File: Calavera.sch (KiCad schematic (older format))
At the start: 21 parts, among them Q1 Q_DUAL_NMOS, U1 AT42QT1012, U2 LMV932

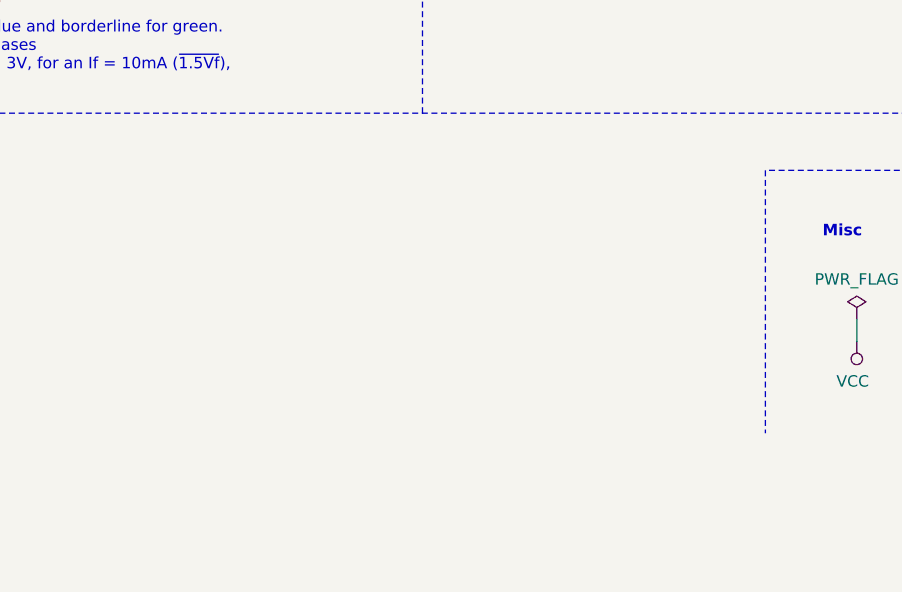
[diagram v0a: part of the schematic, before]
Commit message: Added Silk, Mask and Edge as schematic symbols Updated silk and mask, as they got misaligned Added silk to the nose pad
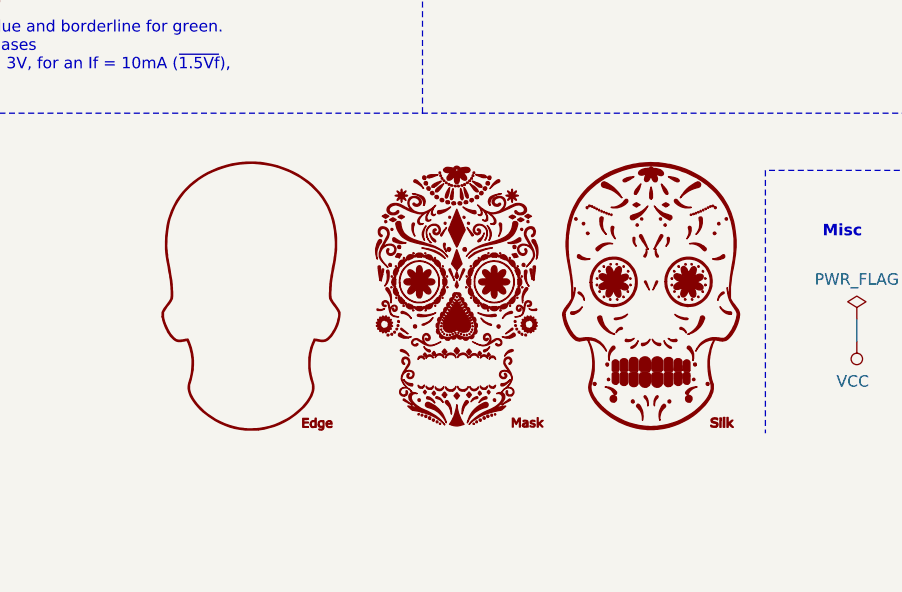
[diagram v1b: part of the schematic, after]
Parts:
- added G2: Edge, Calavera:Calavera_Board_Margins, symbol Calavera:Edge
- added G3: Mask, Calavera:Calavera_SolderMask_1200dpi, symbol Calavera:Mask
- added G4: Silk, Calavera:Calavera_SilkScreen_1200dpi, symbol Calavera:Silk
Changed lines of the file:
@@
 Wire Notes Line
 	500  5100 11200 5100
+$Comp
+L Calavera:Silk G4
+U 1 1 5D5C30EC
+P 9650 5900
+F 0 "G4" H 9650 5339 60  0001 C CNN
+F 1 "Silk" H 9650 6461 60  0001 C CNN
+F 2 "Calavera:Calavera_SilkScreen_1200dpi" H 9650 5900 50  0001 C CNN
+F 3 "" H 9650 5900 50  0001 C CNN
+	1    9650 5900
+	1    0    0    -1
+$EndComp
+$Comp
+L Calavera:Mask G3
+U 1 1 5D5CCE2E
+P 8800 5900
+F 0 "G3" H 9150 5400 60  0001 C CNN
+F 1 "Mask" H 9200 6450 60  0001 C CNN
+F 2 "Calavera:Calavera_SolderMask_1200dpi" H 8800 5900 50  0001 C CNN
+F 3 "" H 8800 5900 50  0001 C CNN
+	1    8800 5900
+	1    0    0    -1
+$EndComp
+$Comp
+L Calavera:Edge G2
+U 1 1 5D5D7396
+P 7900 5900
+F 0 "G2" H 8250 5400 60  0001 C CNN
+F 1 "Edge" H 8300 6450 60  0001 C CNN
+F 2 "Calavera:Calavera_Board_Margins" H 7900 5900 50  0001 C CNN
+F 3 "" H 7900 5900 50  0001 C CNN
+	1    7900 5900
+	1    0    0    -1
+$EndComp
 $EndSCHEMATC

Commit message: v1.0 - Manufactured for the lunch and learn
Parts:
- BT1: MPN (none) -> MP000357; Manufacturer  (none) -> Multicomp
- Q1: MPN (none) -> NX138BKS
- R9: value 2500 -> 2490
- U1: MPN (none) -> AT42QT1012-TSHR
- U2: MPN (none) -> LMV932DR2G
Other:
- note added: "Limiting resistors: voltage is not high enough for Blue and borderline for green.\nI think it's safe to not populate them in these two cases\nTypical red Vf is 1.8V, so in the best case of VDD = 3V, for an If = 10mA (1.5Vf-ish), \nR = 100 to 150Ω"
- note removed: "Limiting resistors: voltage is not high enough for Blue and borderline for green.\nI think it's safe to not populate them in these two cases\nTypical red Vf is 1.8V, so in the best case of VDD = 3V, for an If = 10mA (~1.5Vf), \nR = 150Ω"
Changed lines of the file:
@@
 F 2 "Calavera:CR2032_Multicomp_MP000357_Alternative" V 9450 3960 50  0001 C CNN
 F 3 "~" V 9450 3960 50  0001 C CNN
+F 4 "MP000357" H 9450 3900 50  0001 C CNN "MPN"
+F 5 "Multicomp" H 9450 3900 50  0001 C CNN "Manufacturer "
 	1    9450 3900
 	1    0    0    -1
@@
 F 1 "LMV932" H 8200 2176 50  0000 C CNN
 F 2 "Calavera:SOIC-8_Dual_OpAmp" H 8200 1900 50  0001 C CNN
-F 3 "~" H 8200 1900 50  0001 C CNN
+F 3 "https://www.onsemi.com/pub/Collateral/LMV931-D.PDF" H 8200 1900 50  0001 C CNN
 	2    8200 1900
 	1    0    0    -1
@@
 F 1 "LMV932" H 9208 1655 50  0000 L CNN
 F 2 "Calavera:SOIC-8_Dual_OpAmp" H 9250 1700 50  0001 C CNN
-F 3 "~" H 9250 1700 50  0001 C CNN
+F 3 "https://www.onsemi.com/pub/Collateral/LMV931-D.PDF" H 9250 1700 50  0001 C CNN
 	3    9250 1700
 	1    0    0    -1
@@
 F 1 "LMV932" H 7000 2076 50  0000 C CNN
 F 2 "Calavera:SOIC-8_Dual_OpAmp" H 7000 1800 50  0001 C CNN
-F 3 "~" H 7000 1800 50  0001 C CNN
+F 3 "https://www.onsemi.com/pub/Collateral/LMV931-D.PDF" H 7000 1800 50  0001 C CNN
+F 4 "LMV932DR2G" H 7000 1800 50  0001 C CNN "MPN"
 	1    7000 1800
 	1    0    0    -1
@@
 P 9700 1600
 F 0 "R9" H 9768 1646 50  0000 L CNN
-F 1 "2500" H 9768 1555 50  0000 L CNN
+F 1 "2490" H 9768 1555 50  0000 L CNN
 F 2 "felcana:0805-R_Handsolder" H 9700 1600 50  0001 C CNN
 F 3 "~" H 9700 1600 50  0001 C CNN
@@
 F 1 "Q_DUAL_NMOS" H 4050 3800 50  0001 L CNN
 F 2 "Calavera:SOT-363_NX138BKS_Handsolder" H 4600 3750 50  0001 C CNN
-F 3 "~" H 4050 3900 50  0001 C CNN
+F 3 "https://assets.nexperia.com/documents/data-sheet/NX138BKS.pdf" H 4050 3900 50  0001 C CNN
 	2    3850 3900
 	-1   0    0    -1
@@
 F 1 "Q_DUAL_NMOS" H 3200 3900 50  0001 L CNN
 F 2 "Calavera:SOT-363_NX138BKS_Handsolder" H 3750 3750 50  0001 C CNN
-F 3 "~" H 3200 3900 50  0001 C CNN
+F 3 "https://assets.nexperia.com/documents/data-sheet/NX138BKS.pdf" H 3200 3900 50  0001 C CNN
+F 4 "NX138BKS" H 3000 3900 50  0001 C CNN "MPN"
 	1    3000 3900
 	1    0    0    -1
@@
 VLED
 Text Notes 5050 5000 0    50   ~ 0
-Limiting resistors: voltage is not high enough for Blue and borderline for green.\nI think it's safe to not populate them in these two cases\nTypical red Vf is 1.8V, so in the best case of VDD = 3V, for an If = 10mA (~1.5Vf), \nR = 150Ω
+Limiting resistors: voltage is not high enough for Blue and borderline for green.\nI think it's safe to not populate them in these two cases\nTypical red Vf is 1.8V, so in the best case of VDD = 3V, for an If = 10mA (1.5Vf-ish), \nR = 100 to 150Ω
 Text Notes 9100 4600 0    50   ~ 0
 A lithium coin cell starts at 3V \nand will drop to around 2.5V
@@
 F 1 "AT42QT1012" H 3100 1500 50  0000 C CNN
 F 2 "Calavera:SOT23-6-AT42QT1012" H 2800 1900 50  0001 C CNN
-F 3 "" H 2800 1900 50  0001 C CNN
+F 3 "http://ww1.microchip.com/downloads/en/devicedoc/40001948a.pdf" H 2800 1900 50  0001 C CNN
+F 4 "AT42QT1012-TSHR " H 2800 1900 50  0001 C CNN "MPN"
 	1    2800 1900
 	1    0    0    -1

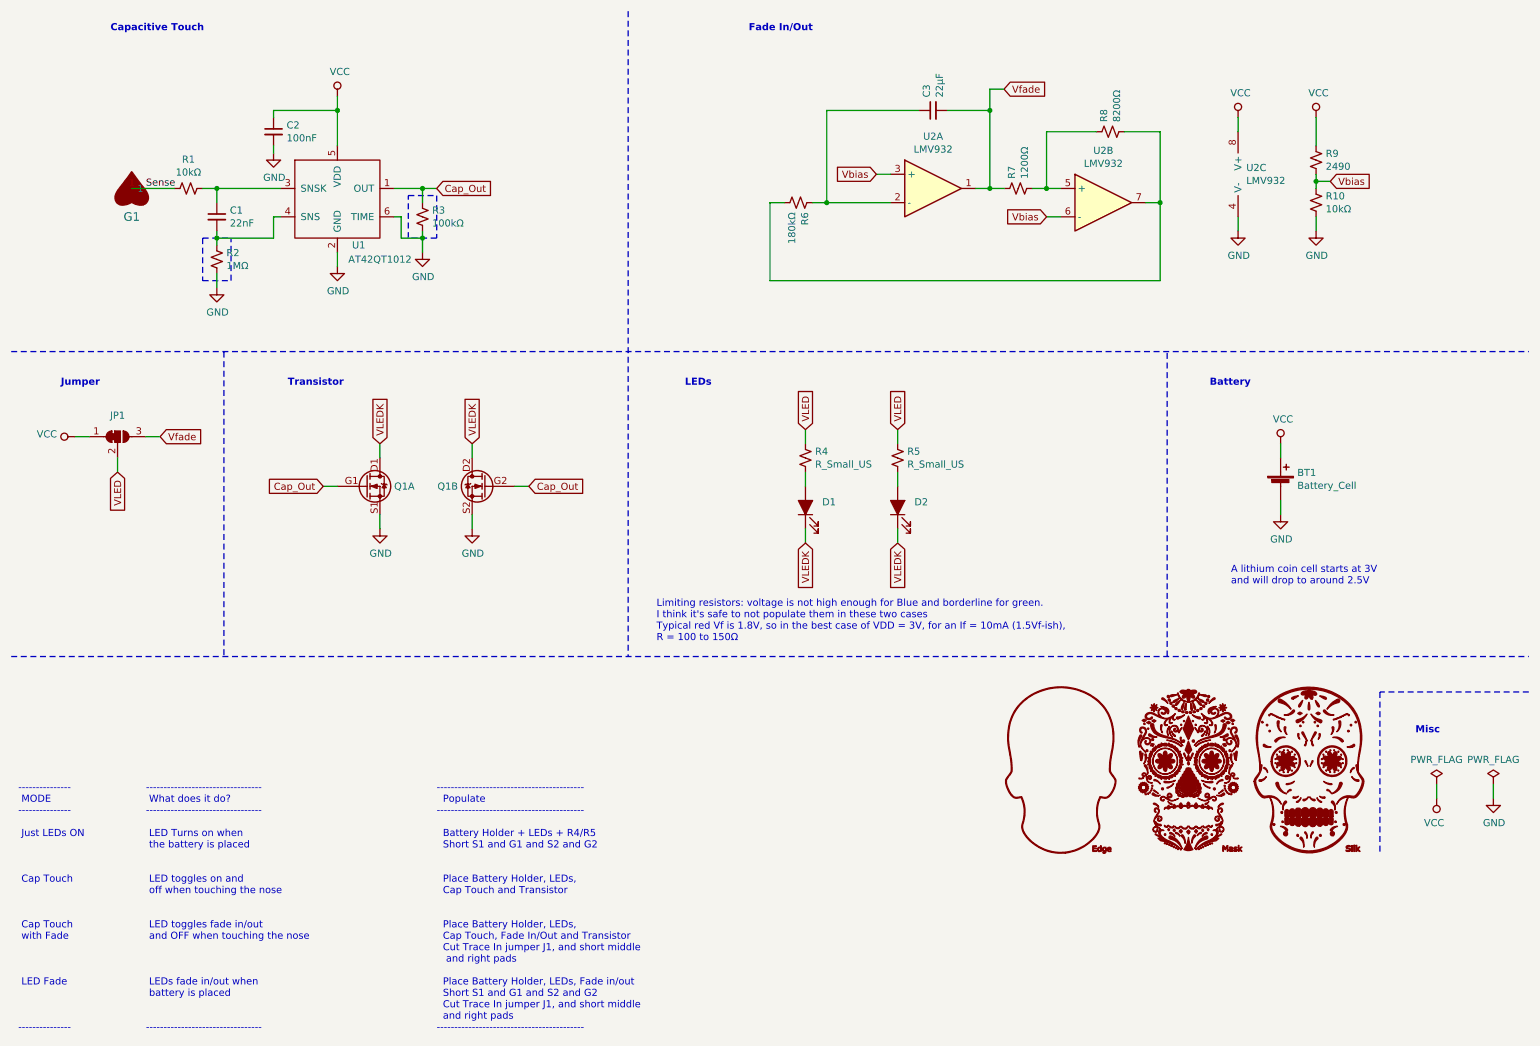
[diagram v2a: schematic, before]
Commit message: Made tracks thicker, as they are easier to rip when overheat than I thought they would be
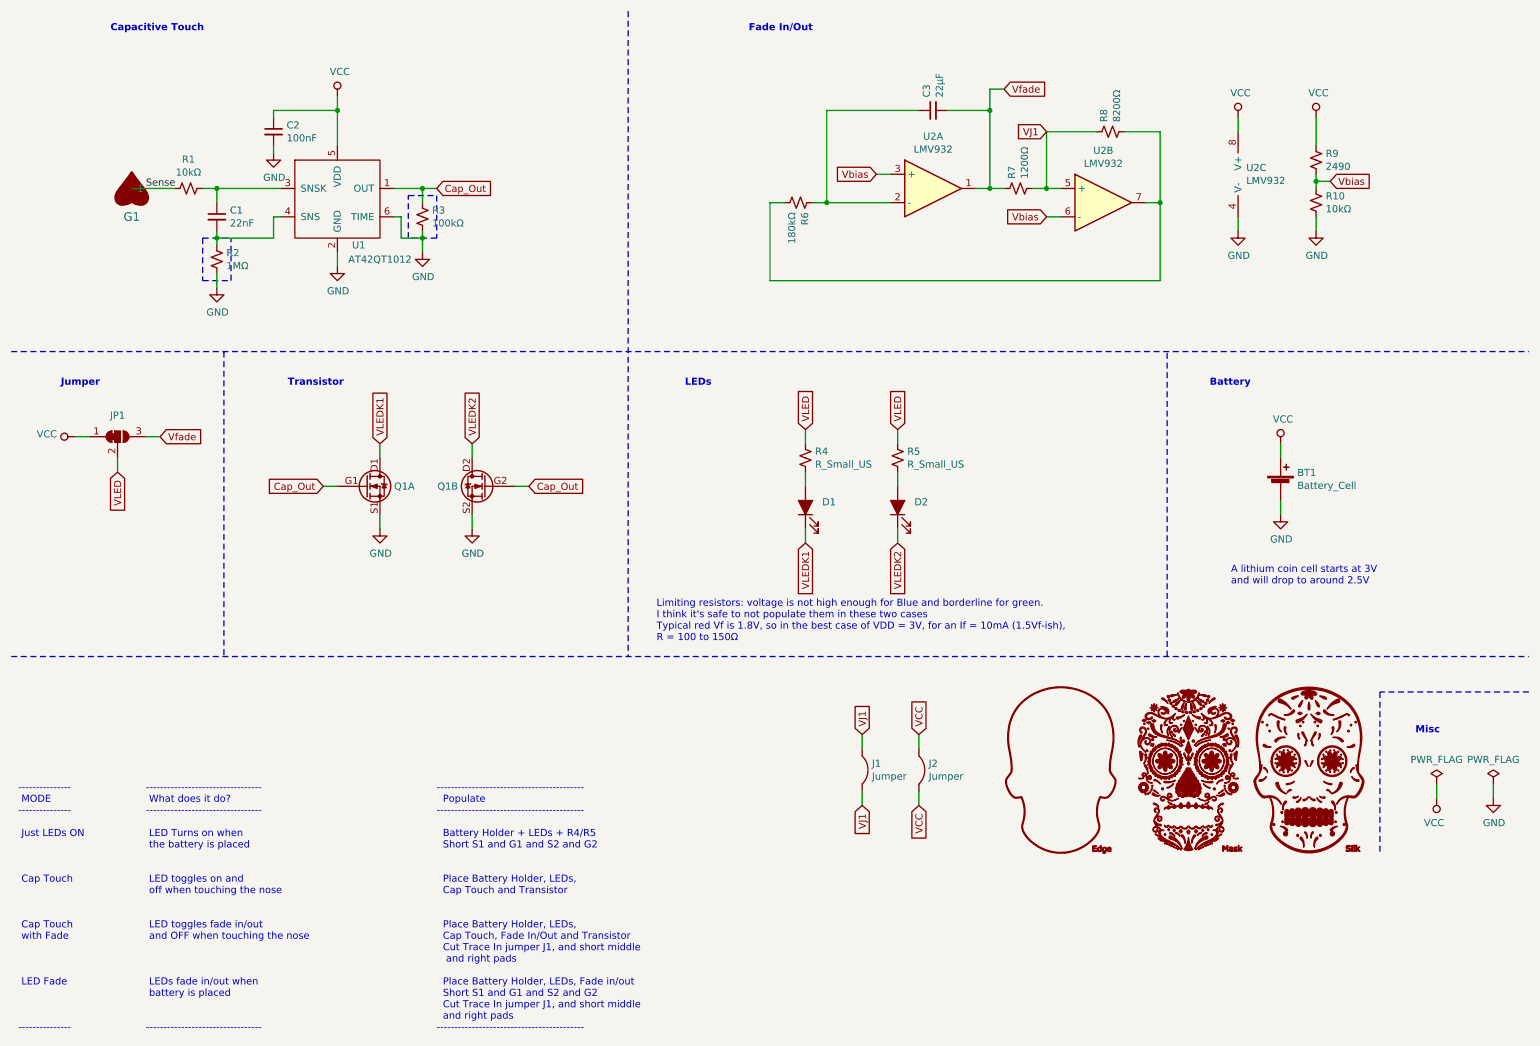
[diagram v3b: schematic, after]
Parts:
- added J1, J2: Jumper, Calavera:Jumper-0805, symbol Calavera:Jumper
- G3: footprint Calavera:Calavera_SolderMask_1200dpi -> Calavera:Calavera_SolderMask_1200dpi_Border
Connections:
- net VCC: now also J2.1
- net VJ1: now reaches R7.2, R8.1, U2.5 (+)
- net VJ1: now also J1.1
- net VLEDK renamed VLEDK1
- net VLEDK1: no longer D2.1 (K), Q1.D2 (D1)
- new net VLEDK2: D2.1 (K), Q1.D2 (D1)
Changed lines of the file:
@@
 EESchema Schematic File Version 4
 LIBS:Calavera-cache
-EELAYER 29 0
+EELAYER 30 0
 EELAYER END
 $Descr A4 11693 8268
@@
 	6750 4200 6750 4300
 Text GLabel 3100 3600 1    50   Input ~ 0
-VLEDK
+VLEDK1
 Text GLabel 3750 3600 1    50   Input ~ 0
-VLEDK
+VLEDK2
 Text GLabel 6100 4300 3    50   Input ~ 0
-VLEDK
+VLEDK1
 Text GLabel 6750 4300 3    50   Input ~ 0
-VLEDK
+VLEDK2
 Text Notes 5700 700  0    50   ~ 10
 Fade In/Out
@@
 F 0 "G3" H 9150 5400 60  0001 C CNN
 F 1 "Mask" H 9200 6450 60  0001 C CNN
-F 2 "Calavera:Calavera_SolderMask_1200dpi" H 8800 5900 50  0001 C CNN
+F 2 "Calavera:Calavera_SolderMask_1200dpi_Border" H 8800 5900 50  0001 C CNN
 F 3 "" H 8800 5900 50  0001 C CNN
 	1    8800 5900
@@
 	1    0    0    -1
 $EndComp
+$Comp
+L Calavera:Jumper J2
+U 1 1 5E17F6F3
+P 6900 5900
+F 0 "J2" V 6854 5969 50  0000 L CNN
+F 1 "Jumper" V 6945 5969 50  0000 L CNN
+F 2 "Calavera:Jumper-0805" H 6900 5900 50  0001 C CNN
+F 3 "" H 6900 5900 50  0001 C CNN
+	1    6900 5900
+	0    1    1    0
+$EndComp
+Wire Wire Line
+	6900 5750 6900 5650
+Wire Wire Line
+	6900 6050 6900 6150
+Text GLabel 6900 5650 1    50   Input ~ 0
+VCC
+Text GLabel 6900 6150 3    50   Input ~ 0
+VCC
+$Comp
+L Calavera:Jumper J1
+U 1 1 5E186C8E
+P 6500 5900
+F 0 "J1" V 6454 5969 50  0000 L CNN
+F 1 "Jumper" V 6545 5969 50  0000 L CNN
+F 2 "Calavera:Jumper-0805" H 6500 5900 50  0001 C CNN
+F 3 "" H 6500 5900 50  0001 C CNN
+	1    6500 5900
+	0    1    1    0
+$EndComp
+Wire Wire Line
+	6500 5750 6500 5650
+Wire Wire Line
+	6500 6050 6500 6150
+Text GLabel 6500 5650 1    50   Input ~ 0
+VJ1
+Text GLabel 6500 6150 3    50   Input ~ 0
+VJ1
+Text GLabel 7800 1400 0    50   Input ~ 0
+VJ1
 $EndSCHEMATC

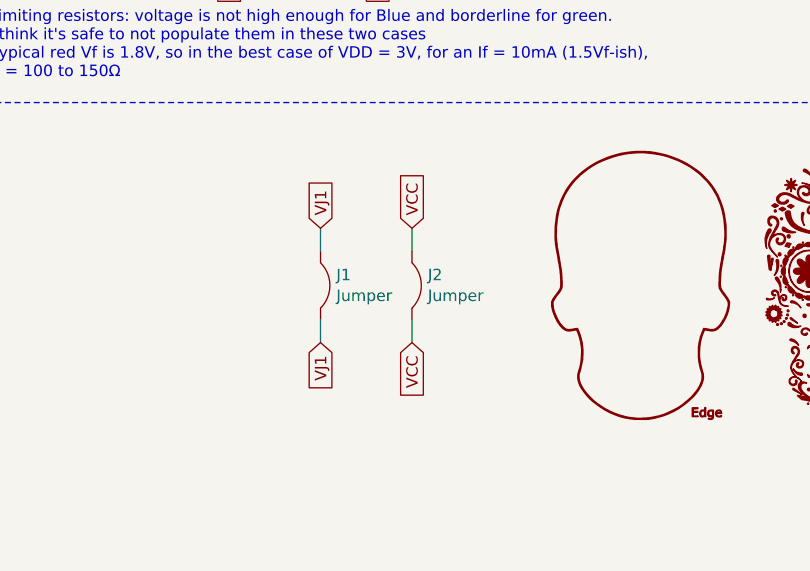
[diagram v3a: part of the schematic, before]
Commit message: Removed the Jumpers as they are not needed
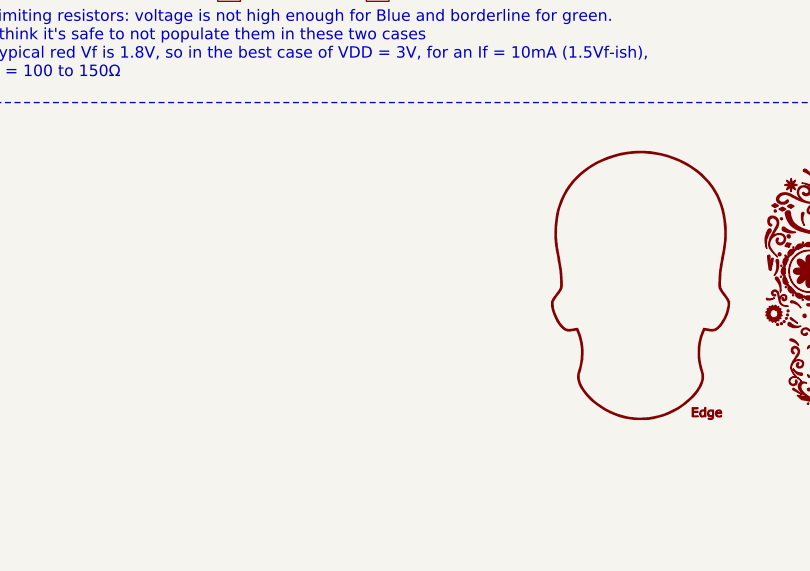
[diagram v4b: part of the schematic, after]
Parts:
- removed J1, J2: Jumper, Calavera:Jumper-0805, symbol Calavera:Jumper
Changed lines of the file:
@@
 	1    0    0    -1
 $EndComp
-$Comp
-L Calavera:Jumper J2
-U 1 1 5E17F6F3
-P 6900 5900
-F 0 "J2" V 6854 5969 50  0000 L CNN
-F 1 "Jumper" V 6945 5969 50  0000 L CNN
-F 2 "Calavera:Jumper-0805" H 6900 5900 50  0001 C CNN
-F 3 "" H 6900 5900 50  0001 C CNN
-	1    6900 5900
-	0    1    1    0
-$EndComp
-Wire Wire Line
-	6900 5750 6900 5650
-Wire Wire Line
-	6900 6050 6900 6150
-Text GLabel 6900 5650 1    50   Input ~ 0
-VCC
-Text GLabel 6900 6150 3    50   Input ~ 0
-VCC
-$Comp
-L Calavera:Jumper J1
-U 1 1 5E186C8E
-P 6500 5900
-F 0 "J1" V 6454 5969 50  0000 L CNN
-F 1 "Jumper" V 6545 5969 50  0000 L CNN
-F 2 "Calavera:Jumper-0805" H 6500 5900 50  0001 C CNN
-F 3 "" H 6500 5900 50  0001 C CNN
-	1    6500 5900
-	0    1    1    0
-$EndComp
-Wire Wire Line
-	6500 5750 6500 5650
-Wire Wire Line
-	6500 6050 6500 6150
-Text GLabel 6500 5650 1    50   Input ~ 0
-VJ1
-Text GLabel 6500 6150 3    50   Input ~ 0
-VJ1
 Text GLabel 7800 1400 0    50   Input ~ 0
 VJ1

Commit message: Changed the transistor footprint to a SOT23 as it was very tricky to solder.
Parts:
- Q1: footprint Calavera:SOT-363_NX138BKS_Handsolder -> Calavera:SOT23-6-NMOSx2_Handsolder
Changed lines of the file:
@@
 F 0 "Q1" H 4050 3900 50  0000 L CNN
 F 1 "Q_DUAL_NMOS" H 4050 3800 50  0001 L CNN
-F 2 "Calavera:SOT-363_NX138BKS_Handsolder" H 4600 3750 50  0001 C CNN
+F 2 "Calavera:SOT23-6-NMOSx2_Handsolder" H 4600 3750 50  0001 C CNN
 F 3 "https://assets.nexperia.com/documents/data-sheet/NX138BKS.pdf" H 4050 3900 50  0001 C CNN
 	2    3850 3900
@@
 F 0 "Q1" H 3200 3900 50  0000 L CNN
 F 1 "Q_DUAL_NMOS" H 3200 3900 50  0001 L CNN
-F 2 "Calavera:SOT-363_NX138BKS_Handsolder" H 3750 3750 50  0001 C CNN
+F 2 "Calavera:SOT23-6-NMOSx2_Handsolder" H 3750 3750 50  0001 C CNN
 F 3 "https://assets.nexperia.com/documents/data-sheet/NX138BKS.pdf" H 3200 3900 50  0001 C CNN
 F 4 "NX138BKS" H 3000 3900 50  0001 C CNN "MPN"
